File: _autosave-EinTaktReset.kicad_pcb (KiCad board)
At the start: 2 copper layers, 100 x 160 mm, 59 parts, among them IC1 74LS624, J1 3PinTerminalBlocktg, J2 3PinTerminalBlocktg, J3 2PinTerminalBlocktg, J4 3PinTerminalBlocktg, J5 2PinTerminalBlocktg, P1 CONN_02X10, P4 CONN_02X10, SW1 SWITCH_INV, SW10 SPST, SW11 SPST, SW12 SPST, SW13 SPST, SW2 SWITCH_INV, SW3 SPST, SW4 SPST, SW5 SPST, SW6 SWITCH_INV, SW7 SPST, SW8 SPST, SW9 SPST, U1 74LS132, U2 74540En, U3 74HCT541_PWR, U4 74LS32, U5 74LS00

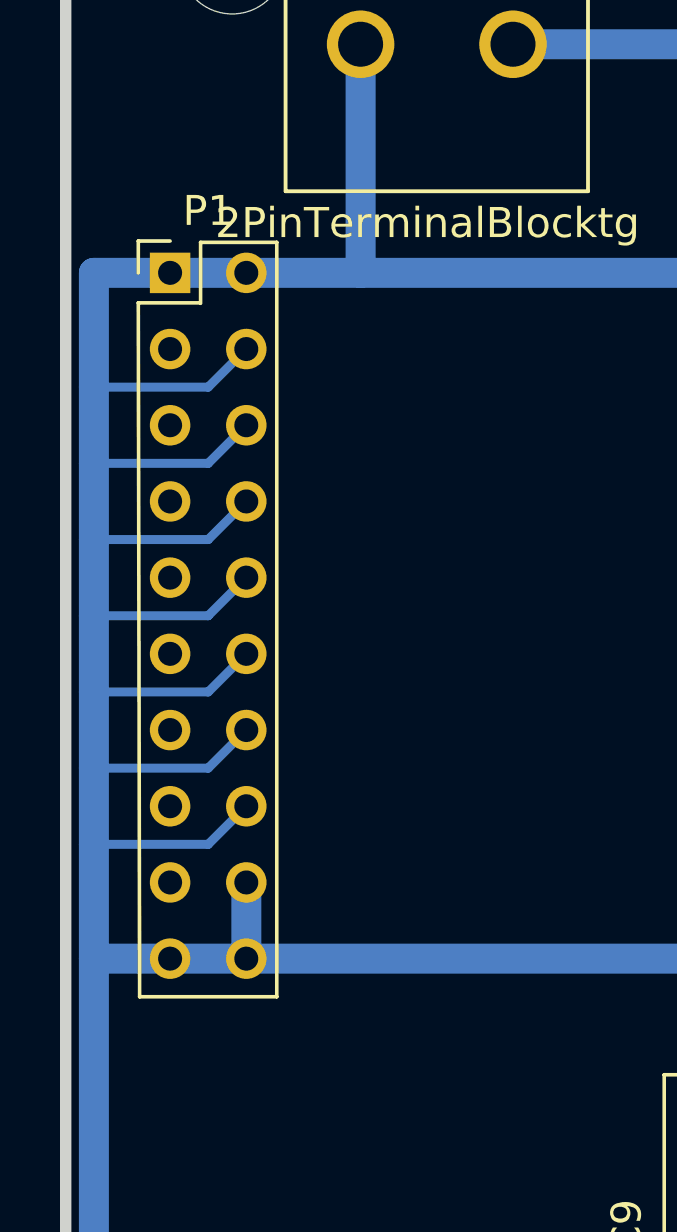
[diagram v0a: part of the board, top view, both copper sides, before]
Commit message: EinTaktReset: weiter Verbindungen gelegt, BUSCONNECTOR LINKS VERDREHT, todo updated
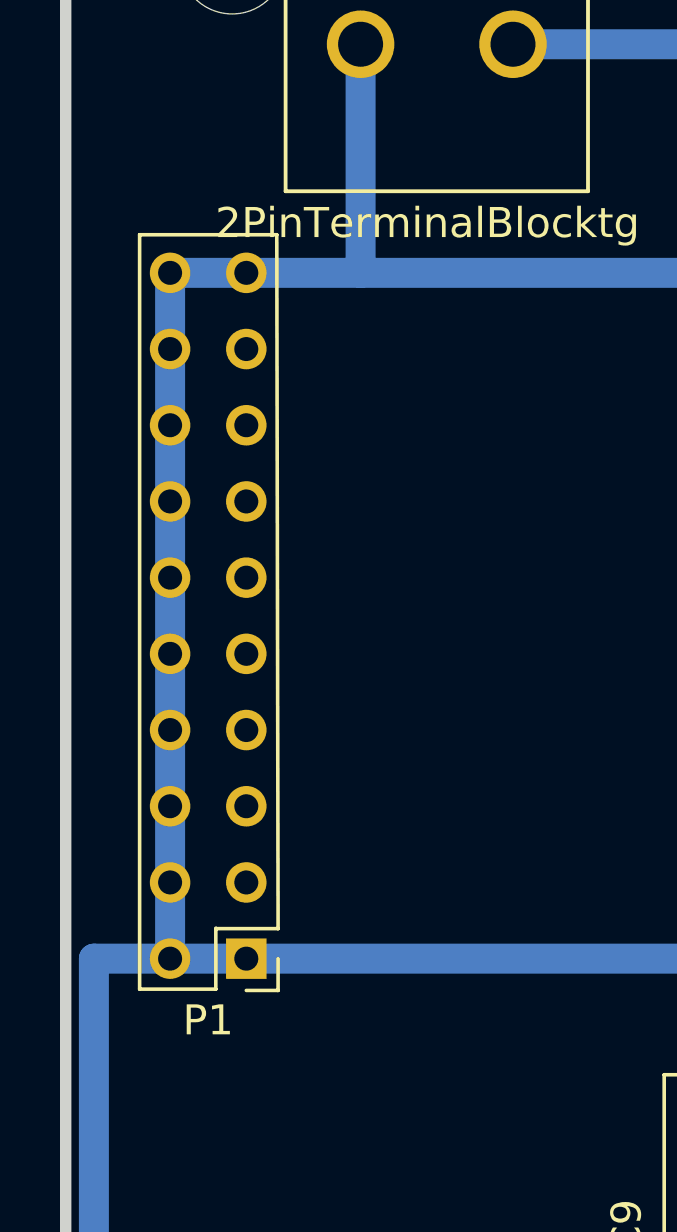
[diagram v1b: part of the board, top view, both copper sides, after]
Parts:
- moved P1 23.0 mm to (15.2, 77.5), turned to 180 degrees
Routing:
- net GND: track 619.9 -> 575.6 mm
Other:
- net class Default: trace_width 1 -> 0.3
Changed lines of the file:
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@@
   (general
     (links 185)
-    (no_connects 105)
+    (no_connects 114)
     (area 0 0 0 0)
     (thickness 1.6)
     (drawings 0)
-    (tracks 254)
+    (tracks 230)
     (zones 0)
     (modules 59)
@@
   )
   (setup
-    (last_trace_width 1)
+    (last_trace_width 0.3)
     (trace_clearance 0.2)
     (zone_clearance 0.508)
@@
   (net_class Default "This is the default net class."
     (clearance 0.2)
-    (trace_width 1)
+    (trace_width 0.3)
     (via_dia 0.8)
     (via_drill 0.4)
@@
   )
   (module tg_foodprint:Pin_Header_Straight_2x10_Pitch2.00mmBonsai.pretty (layer F.Cu)
-    (at 12.7 54.61)
+    (at 15.24 77.47 180)
     (descr "Through hole straight pin header, 2x10, 2.00mm pitch, double rows")
     (tags "Through hole pin header THT 2x10 2.00mm double row")
-    (fp_text reference P1 (at 1.27 -2.06) (layer F.SilkS)
+    (fp_text reference P1 (at 1.27 -2.06 180) (layer F.SilkS)
       (effects (font (size 1 1) (thickness 0.15)))
     )
-    (fp_text value CONN_02X10 (at 1 25.4) (layer F.Fab)
+    (fp_text value CONN_02X10 (at 1 25.4 180) (layer F.Fab)
       (effects (font (size 1 1) (thickness 0.15)))
     )
-    (fp_text user %R (at 1 21.7 90) (layer F.Fab)
+    (fp_text user %R (at 1 21.7 270) (layer F.Fab)
       (effects (font (size 1 1) (thickness 0.15)))
     )
@@
     (fp_line (start 3.556 -1.016) (end 3.556 24.13) (layer F.Fab) (width 0.1))
     (fp_line (start 0 -1.016) (end 3.556 -1.016) (layer F.Fab) (width 0.1))
-    (pad 20 thru_hole oval (at 2.54 22.86) (size 1.35 1.35) (drill 0.8) (layers *.Cu *.Mask)
+    (pad 20 thru_hole oval (at 2.54 22.86 180) (size 1.35 1.35) (drill 0.8) (layers *.Cu *.Mask)
       (net 12 GND))
-    (pad 10 thru_hole oval (at 0 22.86) (size 1.35 1.35) (drill 0.8) (layers *.Cu *.Mask)
+    (pad 10 thru_hole oval (at 0 22.86 180) (size 1.35 1.35) (drill 0.8) (layers *.Cu *.Mask)
       (net 12 GND))
-    (pad 19 thru_hole oval (at 2.54 20.32) (size 1.35 1.35) (drill 0.8) (layers *.Cu *.Mask)
+    (pad 19 thru_hole oval (at 2.54 20.32 180) (size 1.35 1.35) (drill 0.8) (layers *.Cu *.Mask)
       (net 12 GND))
-    (pad 9 thru_hole oval (at 0 20.32) (size 1.35 1.35) (drill 0.8) (layers *.Cu *.Mask)
+    (pad 9 thru_hole oval (at 0 20.32 180) (size 1.35 1.35) (drill 0.8) (layers *.Cu *.Mask)
       (net 34 /a7))
-    (pad 18 thru_hole oval (at 2.54 17.78) (size 1.35 1.35) (drill 0.8) (layers *.Cu *.Mask)
+    (pad 18 thru_hole oval (at 2.54 17.78 180) (size 1.35 1.35) (drill 0.8) (layers *.Cu *.Mask)
       (net 12 GND))
-    (pad 8 thru_hole oval (at 0 17.78) (size 1.35 1.35) (drill 0.8) (layers *.Cu *.Mask)
+    (pad 8 thru_hole oval (at 0 17.78 180) (size 1.35 1.35) (drill 0.8) (layers *.Cu *.Mask)
       (net 32 /a6))
-    (pad 17 thru_hole oval (at 2.54 15.24) (size 1.35 1.35) (drill 0.8) (layers *.Cu *.Mask)
+    (pad 17 thru_hole oval (at 2.54 15.24 180) (size 1.35 1.35) (drill 0.8) (layers *.Cu *.Mask)
       (net 12 GND))
-    (pad 7 thru_hole oval (at 0 15.24) (size 1.35 1.35) (drill 0.8) (layers *.Cu *.Mask)
+    (pad 7 thru_hole oval (at 0 15.24 180) (size 1.35 1.35) (drill 0.8) (layers *.Cu *.Mask)
       (net 30 /a5))
-    (pad 16 thru_hole oval (at 2.54 12.7) (size 1.35 1.35) (drill 0.8) (layers *.Cu *.Mask)
+    (pad 16 thru_hole oval (at 2.54 12.7 180) (size 1.35 1.35) (drill 0.8) (layers *.Cu *.Mask)
       (net 12 GND))
-    (pad 6 thru_hole oval (at 0 12.7) (size 1.35 1.35) (drill 0.8) (layers *.Cu *.Mask)
+    (pad 6 thru_hole oval (at 0 12.7 180) (size 1.35 1.35) (drill 0.8) (layers *.Cu *.Mask)
       (net 28 /a4))
-    (pad 15 thru_hole oval (at 2.54 10.16) (size 1.35 1.35) (drill 0.8) (layers *.Cu *.Mask)
+    (pad 15 thru_hole oval (at 2.54 10.16 180) (size 1.35 1.35) (drill 0.8) (layers *.Cu *.Mask)
       (net 12 GND))
-    (pad 5 thru_hole oval (at 0 10.16) (size 1.35 1.35) (drill 0.8) (layers *.Cu *.Mask)
+    (pad 5 thru_hole oval (at 0 10.16 180) (size 1.35 1.35) (drill 0.8) (layers *.Cu *.Mask)
       (net 26 /a3))
-    (pad 14 thru_hole oval (at 2.54 7.62) (size 1.35 1.35) (drill 0.8) (layers *.Cu *.Mask)
+    (pad 14 thru_hole oval (at 2.54 7.62 180) (size 1.35 1.35) (drill 0.8) (layers *.Cu *.Mask)
       (net 12 GND))
-    (pad 4 thru_hole oval (at 0 7.62) (size 1.35 1.35) (drill 0.8) (layers *.Cu *.Mask)
+    (pad 4 thru_hole oval (at 0 7.62 180) (size 1.35 1.35) (drill 0.8) (layers *.Cu *.Mask)
       (net 24 /a2))
-    (pad 13 thru_hole oval (at 2.54 5.08) (size 1.35 1.35) (drill 0.8) (layers *.Cu *.Mask)
+    (pad 13 thru_hole oval (at 2.54 5.08 180) (size 1.35 1.35) (drill 0.8) (layers *.Cu *.Mask)
       (net 12 GND))
-    (pad 3 thru_hole oval (at 0 5.08) (size 1.35 1.35) (drill 0.8) (layers *.Cu *.Mask)
+    (pad 3 thru_hole oval (at 0 5.08 180) (size 1.35 1.35) (drill 0.8) (layers *.Cu *.Mask)
       (net 22 /a1))
-    (pad 12 thru_hole oval (at 2.54 2.54) (size 1.35 1.35) (drill 0.8) (layers *.Cu *.Mask)
+    (pad 12 thru_hole oval (at 2.54 2.54 180) (size 1.35 1.35) (drill 0.8) (layers *.Cu *.Mask)
       (net 12 GND))
-    (pad 2 thru_hole oval (at 0 2.54) (size 1.35 1.35) (drill 0.8) (layers *.Cu *.Mask)
+    (pad 2 thru_hole oval (at 0 2.54 180) (size 1.35 1.35) (drill 0.8) (layers *.Cu *.Mask)
       (net 20 /a0))
-    (pad 11 thru_hole oval (at 2.54 0) (size 1.35 1.35) (drill 0.8) (layers *.Cu *.Mask)
+    (pad 11 thru_hole oval (at 2.54 0 180) (size 1.35 1.35) (drill 0.8) (layers *.Cu *.Mask)
       (net 12 GND))
-    (pad 1 thru_hole rect (at 0 0) (size 1.35 1.35) (drill 0.8) (layers *.Cu *.Mask)
+    (pad 1 thru_hole rect (at 0 0 180) (size 1.35 1.35) (drill 0.8) (layers *.Cu *.Mask)
       (net 12 GND))
     (model ${KISYS3DMOD}/Pin_Headers.3dshapes/Pin_Header_Straight_2x10_Pitch2.00mm.wrl
@@
   (segment (start 71.12 186.69) (end 71.12 179.07) (width 0.5) (layer B.Cu) (net 9))
   (segment (start 71.12 179.07) (end 71.12 175.26) (width 0.5) (layer B.Cu) (net 9))
-  (segment (start 101.6 54.61) (end 99.06 54.61) (width 1) (layer B.Cu) (net 12) (status C00000))
-  (segment (start 101.6 77.47) (end 78.74 77.47) (width 1) (layer B.Cu) (net 12) (status 400000))
+  (segment (start 12.7 77.47) (end 12.7 54.61) (width 1) (layer B.Cu) (net 12) (status C00000))
+  (segment (start 12.7 54.61) (end 19.05 54.61) (width 1) (layer B.Cu) (net 12) (status 400000))
+  (segment (start 101.6 54.61) (end 99.06 54.61) (width 1) (layer B.Cu) (net 12))
+  (segment (start 101.6 77.47) (end 78.74 77.47) (width 1) (layer B.Cu) (net 12))
   (segment (start 78.74 77.47) (end 15.24 77.47) (width 1) (layer B.Cu) (net 12))
-  (segment (start 101.6 77.47) (end 101.6 54.61) (width 1) (layer B.Cu) (net 12) (status 400000))
-  (segment (start 15.24 77.47) (end 15.24 74.93) (width 1) (layer B.Cu) (net 12) (status C00000))
-  (segment (start 10.16 58.42) (end 13.97 58.42) (width 0.3) (layer B.Cu) (net 12))
-  (segment (start 13.97 58.42) (end 15.24 57.15) (width 0.3) (layer B.Cu) (net 12) (status 800000))
-  (segment (start 10.16 60.96) (end 13.97 60.96) (width 0.3) (layer B.Cu) (net 12))
-  (segment (start 13.97 60.96) (end 15.24 59.69) (width 0.3) (layer B.Cu) (net 12) (status 800000))
-  (segment (start 10.16 63.5) (end 13.97 63.5) (width 0.3) (layer B.Cu) (net 12))
-  (segment (start 13.97 63.5) (end 15.24 62.23) (width 0.3) (layer B.Cu) (net 12) (status 800000))
-  (segment (start 10.16 66.04) (end 13.97 66.04) (width 0.3) (layer B.Cu) (net 12))
-  (segment (start 13.97 66.04) (end 15.24 64.77) (width 0.3) (layer B.Cu) (net 12) (status 800000))
-  (segment (start 10.16 68.58) (end 13.97 68.58) (width 0.3) (layer B.Cu) (net 12))
-  (segment (start 13.97 68.58) (end 15.24 67.31) (width 0.3) (layer B.Cu) (net 12) (status 800000))
-  (segment (start 10.16 71.12) (end 13.97 71.12) (width 0.3) (layer B.Cu) (net 12))
-  (segment (start 13.97 71.12) (end 15.24 69.85) (width 0.3) (layer B.Cu) (net 12) (status 800000))
-  (segment (start 10.16 73.66) (end 13.97 73.66) (width 0.3) (layer B.Cu) (net 12))
-  (segment (start 13.97 73.66) (end 15.24 72.39) (width 0.3) (layer B.Cu) (net 12) (status 800000))
+  (segment (start 101.6 77.47) (end 101.6 54.61) (width 1) (layer B.Cu) (net 12))
   (segment (start 107.95 142.24) (end 107.95 199.39) (width 1) (layer B.Cu) (net 12))
   (segment (start 107.95 199.39) (end 95.25 199.39) (width 1) (layer B.Cu) (net 12))
@@
   (segment (start 19.05 54.61) (end 40.64 54.61) (width 1) (layer B.Cu) (net 12))
   (segment (start 40.64 54.61) (end 40.64 46.99) (width 1) (layer B.Cu) (net 12))
-  (segment (start 15.24 54.61) (end 19.05 54.61) (width 1) (layer B.Cu) (net 12))
   (segment (start 19.05 54.61) (end 19.05 46.99) (width 1) (layer B.Cu) (net 12))
-  (segment (start 15.24 54.61) (end 12.7 54.61) (width 1) (layer B.Cu) (net 12))
-  (segment (start 12.7 54.61) (end 10.16 54.61) (width 1) (layer B.Cu) (net 12))
-  (segment (start 10.16 54.61) (end 10.16 58.42) (width 1) (layer B.Cu) (net 12))
-  (segment (start 10.16 58.42) (end 10.16 60.96) (width 1) (layer B.Cu) (net 12))
-  (segment (start 10.16 60.96) (end 10.16 63.5) (width 1) (layer B.Cu) (net 12))
-  (segment (start 10.16 63.5) (end 10.16 66.04) (width 1) (layer B.Cu) (net 12))
-  (segment (start 10.16 66.04) (end 10.16 68.58) (width 1) (layer B.Cu) (net 12))
-  (segment (start 10.16 68.58) (end 10.16 71.12) (width 1) (layer B.Cu) (net 12))
-  (segment (start 10.16 71.12) (end 10.16 73.66) (width 1) (layer B.Cu) (net 12))
-  (segment (start 10.16 73.66) (end 10.16 77.47) (width 1) (layer B.Cu) (net 12))
   (segment (start 10.16 77.47) (end 12.7 77.47) (width 1) (layer B.Cu) (net 12))
   (segment (start 12.7 77.47) (end 15.24 77.47) (width 1) (layer B.Cu) (net 12))
